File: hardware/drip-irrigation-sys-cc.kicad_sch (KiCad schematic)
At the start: 4 parts

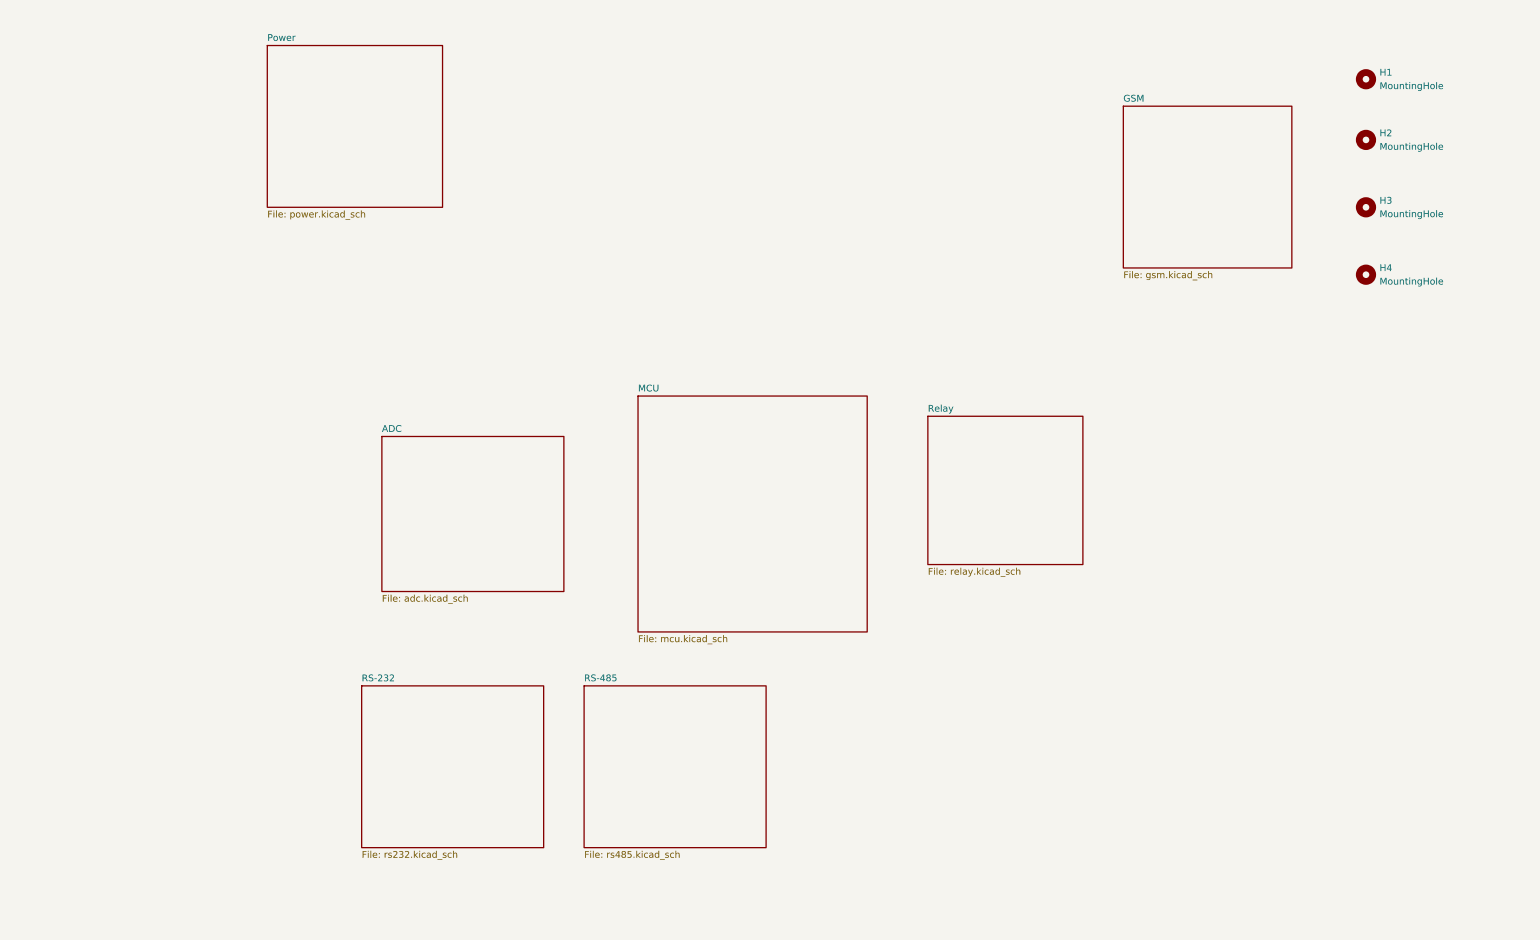
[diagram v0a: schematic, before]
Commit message: power.kicad_sch düzenlemesi yapıldı.
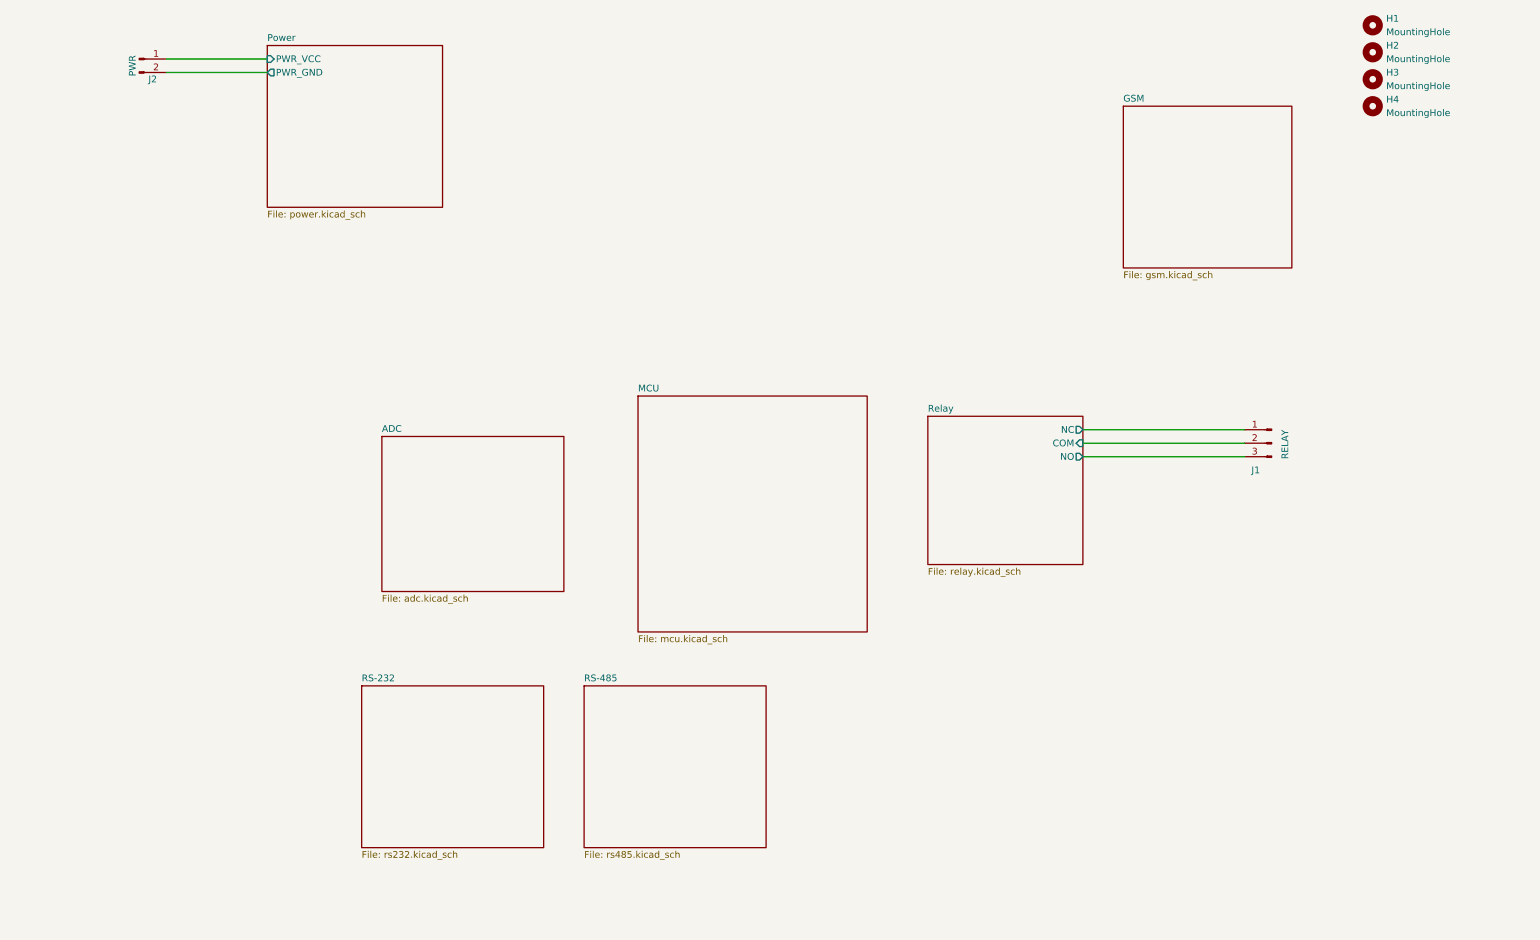
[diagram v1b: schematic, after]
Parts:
- added J1: RELAY, Connector_Phoenix_MSTB:PhoenixContact_MSTBA_2,5_3-G_1x03_P5.00mm_Horizontal, symbol Connector:Conn_01x03_Pin
- added J2: PWR, Connector_Phoenix_MSTB:PhoenixContact_MSTBA_2,5_2-G-5,08_1x02_P5.08mm_Horizontal, symbol Connector:Conn_01x02_Pin
- H1, H2, H3, H4: footprint (none) -> MountingHole:MountingHole_2.5mm
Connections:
- new net Power/PWR_GND: J2.2 (Pin_2)
- new net Power/PWR_VCC: J2.1 (Pin_1)
- new net Relay/COM: J1.2 (Pin_2)
- new net Relay/NC: J1.1 (Pin_1)
- new net Relay/NO: J1.3 (Pin_3)
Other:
- sheet Power ports: added PWR_GND, PWR_VCC; removed none
- sheet Relay ports: added COM, NC, NO; removed none
- moved on the sheet: H1, H2, H3, H4
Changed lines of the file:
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@@
 (kicad_sch (version 20230121) (generator eeschema)
   (paper "A4")
-  (symbol (lib_id "Mechanical:MountingHole") (at 265.43 50.8 0) (unit 1)
-    (in_bom yes) (on_board yes) (dnp no) (fields_autoplaced)
-    (property "Reference" "H3" (at 267.97 49.53 0)
-      (effects (font (size 1.27 1.27)) (justify left))
-    )
-    (property "Value" "MountingHole" (at 267.97 52.07 0)
-      (effects (font (size 1.27 1.27)) (justify left))
-    )
-    (property "Footprint" "" (at 265.43 50.8 0)
-      (effects (font (size 1.27 1.27)) hide)
-    )
-    (property "Datasheet" "~" (at 265.43 50.8 0)
+  (wire (pts (xy 212.09 92.71) (xy 242.57 92.71))
+    (stroke (width 0) (type default))
+  )
+  (wire (pts (xy 212.09 95.25) (xy 242.57 95.25))
+    (stroke (width 0) (type default))
+  )
+  (wire (pts (xy 212.09 97.79) (xy 242.57 97.79))
+    (stroke (width 0) (type default))
+  )
+  (wire (pts (xy 39.37 22.86) (xy 58.42 22.86))
+    (stroke (width 0) (type default))
+  )
+  (wire (pts (xy 39.37 25.4) (xy 58.42 25.4))
+    (stroke (width 0) (type default))
+  )
+  (symbol (lib_id "Mechanical:MountingHole") (at 266.7 26.67 0) (unit 1)
+    (in_bom yes) (on_board yes) (dnp no) (fields_autoplaced)
+    (property "Reference" "H3" (at 269.24 25.4 0)
+      (effects (font (size 1.27 1.27)) (justify left))
+    )
+    (property "Value" "MountingHole" (at 269.24 27.94 0)
+      (effects (font (size 1.27 1.27)) (justify left))
+    )
+    (property "Footprint" "MountingHole:MountingHole_2.5mm" (at 266.7 26.67 0)
+      (effects (font (size 1.27 1.27)) hide)
+    )
+    (property "Datasheet" "~" (at 266.7 26.67 0)
       (effects (font (size 1.27 1.27)) hide)
     )
@@
     )
   )
-  (symbol (lib_id "Mechanical:MountingHole") (at 265.43 63.5 0) (unit 1)
-    (in_bom yes) (on_board yes) (dnp no) (fields_autoplaced)
-    (property "Reference" "H4" (at 267.97 62.23 0)
-      (effects (font (size 1.27 1.27)) (justify left))
-    )
-    (property "Value" "MountingHole" (at 267.97 64.77 0)
-      (effects (font (size 1.27 1.27)) (justify left))
-    )
-    (property "Footprint" "" (at 265.43 63.5 0)
-      (effects (font (size 1.27 1.27)) hide)
-    )
-    (property "Datasheet" "~" (at 265.43 63.5 0)
+  (symbol (lib_id "Connector:Conn_01x02_Pin") (at 34.29 22.86 0) (unit 1)
+    (in_bom yes) (on_board yes) (dnp no)
+    (property "Reference" "J2" (at 36.83 26.67 0)
+      (effects (font (size 1.27 1.27)))
+    )
+    (property "Value" "PWR" (at 33.02 24.13 90)
+      (effects (font (size 1.27 1.27)))
+    )
+    (property "Footprint" "Connector_Phoenix_MSTB:PhoenixContact_MSTBA_2,5_2-G-5,08_1x02_P5.08mm_Horizontal" (at 34.29 22.86 0)
+      (effects (font (size 1.27 1.27)) hide)
+    )
+    (property "Datasheet" "~" (at 34.29 22.86 0)
+      (effects (font (size 1.27 1.27)) hide)
+    )
+    (pin "1")
+    (pin "2")
+    (instances
+      (project "drip-irrigation-sys-cc"
+        (path "/41708c1e-19b2-4374-83f2-108076d82b45"
+          (reference "J2") (unit 1)
+        )
+      )
+    )
+  )
+  (symbol (lib_id "Connector:Conn_01x03_Pin") (at 247.65 95.25 0) (mirror y) (unit 1)
+    (in_bom yes) (on_board yes) (dnp no)
+    (property "Reference" "J1" (at 243.84 100.33 0)
+      (effects (font (size 1.27 1.27)) (justify right))
+    )
+    (property "Value" "RELAY" (at 250.19 92.71 90)
+      (effects (font (size 1.27 1.27)) (justify right))
+    )
+    (property "Footprint" "Connector_Phoenix_MSTB:PhoenixContact_MSTBA_2,5_3-G_1x03_P5.00mm_Horizontal" (at 247.65 95.25 0)
+      (effects (font (size 1.27 1.27)) hide)
+    )
+    (property "Datasheet" "~" (at 247.65 95.25 0)
+      (effects (font (size 1.27 1.27)) hide)
+    )
+    (pin "1")
+    (pin "2")
+    (pin "3")
+    (instances
+      (project "drip-irrigation-sys-cc"
+        (path "/41708c1e-19b2-4374-83f2-108076d82b45"
+          (reference "J1") (unit 1)
+        )
+      )
+    )
+  )
+  (symbol (lib_id "Mechanical:MountingHole") (at 266.7 31.75 0) (unit 1)
+    (in_bom yes) (on_board yes) (dnp no) (fields_autoplaced)
+    (property "Reference" "H4" (at 269.24 30.48 0)
+      (effects (font (size 1.27 1.27)) (justify left))
+    )
+    (property "Value" "MountingHole" (at 269.24 33.02 0)
+      (effects (font (size 1.27 1.27)) (justify left))
+    )
+    (property "Footprint" "MountingHole:MountingHole_2.5mm" (at 266.7 31.75 0)
+      (effects (font (size 1.27 1.27)) hide)
+    )
+    (property "Datasheet" "~" (at 266.7 31.75 0)
       (effects (font (size 1.27 1.27)) hide)
     )
@@
     )
   )
-  (symbol (lib_id "Mechanical:MountingHole") (at 265.43 26.67 0) (unit 1)
-    (in_bom yes) (on_board yes) (dnp no) (fields_autoplaced)
-    (property "Reference" "H1" (at 267.97 25.4 0)
-      (effects (font (size 1.27 1.27)) (justify left))
-    )
-    (property "Value" "MountingHole" (at 267.97 27.94 0)
-      (effects (font (size 1.27 1.27)) (justify left))
-    )
-    (property "Footprint" "" (at 265.43 26.67 0)
-      (effects (font (size 1.27 1.27)) hide)
-    )
-    (property "Datasheet" "~" (at 265.43 26.67 0)
+  (symbol (lib_id "Mechanical:MountingHole") (at 266.7 16.51 0) (unit 1)
+    (in_bom yes) (on_board yes) (dnp no) (fields_autoplaced)
+    (property "Reference" "H1" (at 269.24 15.24 0)
+      (effects (font (size 1.27 1.27)) (justify left))
+    )
+    (property "Value" "MountingHole" (at 269.24 17.78 0)
+      (effects (font (size 1.27 1.27)) (justify left))
+    )
+    (property "Footprint" "MountingHole:MountingHole_2.5mm" (at 266.7 16.51 0)
+      (effects (font (size 1.27 1.27)) hide)
+    )
+    (property "Datasheet" "~" (at 266.7 16.51 0)
       (effects (font (size 1.27 1.27)) hide)
     )
@@
     )
   )
-  (symbol (lib_id "Mechanical:MountingHole") (at 265.43 38.1 0) (unit 1)
-    (in_bom yes) (on_board yes) (dnp no) (fields_autoplaced)
-    (property "Reference" "H2" (at 267.97 36.83 0)
-      (effects (font (size 1.27 1.27)) (justify left))
-    )
-    (property "Value" "MountingHole" (at 267.97 39.37 0)
-      (effects (font (size 1.27 1.27)) (justify left))
-    )
-    (property "Footprint" "" (at 265.43 38.1 0)
-      (effects (font (size 1.27 1.27)) hide)
-    )
-    (property "Datasheet" "~" (at 265.43 38.1 0)
+  (symbol (lib_id "Mechanical:MountingHole") (at 266.7 21.59 0) (unit 1)
+    (in_bom yes) (on_board yes) (dnp no) (fields_autoplaced)
+    (property "Reference" "H2" (at 269.24 20.32 0)
+      (effects (font (size 1.27 1.27)) (justify left))
+    )
+    (property "Value" "MountingHole" (at 269.24 22.86 0)
+      (effects (font (size 1.27 1.27)) (justify left))
+    )
+    (property "Footprint" "MountingHole:MountingHole_2.5mm" (at 266.7 21.59 0)
+      (effects (font (size 1.27 1.27)) hide)
+    )
+    (property "Datasheet" "~" (at 266.7 21.59 0)
       (effects (font (size 1.27 1.27)) hide)
     )
@@
       (effects (font (size 1.27 1.27)) (justify left top))
     )
+    (pin "COM" input (at 212.09 95.25 0)
+      (effects (font (size 1.27 1.27)) (justify right))
+    )
+    (pin "NC" output (at 212.09 92.71 0)
+      (effects (font (size 1.27 1.27)) (justify right))
+    )
+    (pin "NO" output (at 212.09 97.79 0)
+      (effects (font (size 1.27 1.27)) (justify right))
+    )
     (instances
       (project "drip-irrigation-sys-cc"
@@
       (effects (font (size 1.27 1.27)) (justify left top))
     )
-    (instances
+    (pin "PWR_VCC" input (at 58.42 22.86 180)
+      (effects (font (size 1.27 1.27)) (justify left))
+    )
+    (pin "PWR_GND" output (at 58.42 25.4 180)
+      (effects (font (size 1.27 1.27)) (justify left))
+    )
+    (instances

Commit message: Kicad şema düzenlemesi yapıldı.
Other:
- sheet ADC ports: added MCU_ADC, PRESSURE_SENSOR_ANALOG_SIGNAL; removed none
- sheet Relay ports: added 5V_GND, 5V_VCC, MCU_RELAY_PIN; removed none
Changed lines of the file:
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@@
       (effects (font (size 1.27 1.27)) (justify right))
+    )
+    (pin "MCU_RELAY_PIN" output (at 182.88 97.79 180)
+      (effects (font (size 1.27 1.27)) (justify left))
+    )
+    (pin "5V_VCC" output (at 182.88 92.71 180)
+      (effects (font (size 1.27 1.27)) (justify left))
+    )
+    (pin "5V_GND" output (at 182.88 95.25 180)
+      (effects (font (size 1.27 1.27)) (justify left))
     )
     (instances
@@
       (effects (font (size 1.27 1.27)) (justify left top))
     )
+    (pin "PRESSURE_SENSOR_ANALOG_SIGNAL" input (at 80.01 96.52 180)
+      (effects (font (size 1.27 1.27)) (justify left))
+    )
+    (pin "MCU_ADC" output (at 114.3 104.14 0)
+      (effects (font (size 1.27 1.27)) (justify right))
+    )
     (instances

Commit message: Kicad şema düzenlemesi yapıldı.
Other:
- sheet Relay ports: added none; removed 5V_GND, 5V_VCC
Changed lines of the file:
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@@
-      (effects (font (size 1.27 1.27)) (justify left))
-    )
-    (pin "5V_VCC" output (at 182.88 92.71 180)
-      (effects (font (size 1.27 1.27)) (justify left))
-    )
-    (pin "5V_GND" output (at 182.88 95.25 180)
       (effects (font (size 1.27 1.27)) (justify left))
     )

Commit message: Kicad şema düzenlemesi yapıldı.
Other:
- removed sheet GSM
- added sheet mg2608 (mg_2608.kicad_sch)
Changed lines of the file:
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@@
-    )
-  )
-  (sheet (at 219.71 31.75) (size 31.75 30.48) (fields_autoplaced)
-    (stroke (width 0.1524) (type solid))
-    (fill (color 0 0 0 0.0000))
-    (property "Sheetname" "GSM" (at 219.71 31.0384 0)
-      (effects (font (size 1.27 1.27)) (justify left bottom))
-    )
-    (property "Sheetfile" "gsm.kicad_sch" (at 219.71 62.8146 0)
-      (effects (font (size 1.27 1.27)) (justify left top))
-    )
-    (instances
-      (project "drip-irrigation-sys-cc"
-        (path "/41708c1e-19b2-4374-83f2-108076d82b45" (page "7"))
-      )
     )
   )
@@
       )
     )
+  )
+  (sheet (at 205.1812 16.5608) (size 48.9204 34.0868) (fields_autoplaced)
+    (stroke (width 0.1524) (type solid))
+    (fill (color 0 0 0 0.0000))
+    (property "Sheetname" "mg2608" (at 205.1812 15.8492 0)
+      (effects (font (size 1.27 1.27)) (justify left bottom))
+    )
+    (property "Sheetfile" "mg_2608.kicad_sch" (at 205.1812 51.2322 0)
+      (effects (font (size 1.27 1.27)) (justify left top))
+    )
+    (pin "4V" input (at 205.1812 23.8252 180)
+      (effects (font (size 1.27 1.27)) (justify left))
+    )
+    (pin "uart1_rx" input (at 205.1812 32.258 180)
+      (effects (font (size 1.27 1.27)) (justify left))
+    )
+    (pin "uart1_tx" input (at 205.1812 39.1668 180)
+      (effects (font (size 1.27 1.27)) (justify left))
+    )
+    (instances
+      (project "mg2608"
+        (path "/63a0379d-fc16-4019-b887-c3021204e6ee" (page "2"))
+      )
+    )

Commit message: Kicad düzenleme.
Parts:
- added C19: 10nf, symbol Device:C
- added D7: ERROR_LED, symbol Device:LED
- added D8: STATUS_LED, symbol Device:LED
- added D9: POWER_LED, symbol Device:LED
- added J3: PRESSURE_SENSOR, Connector_Phoenix_MSTB:PhoenixContact_MSTBA_2,5_3-G_1x03_P5.00mm_Horizontal, symbol Connector:Conn_01x03_Pin
- added J4: USB_A, symbol Connector:USB_A
- added K2, K3: Relay_SPST-NO, symbol Relay:Relay_SPST-NO
- added R14, R15, R16: 100ohm, symbol Device:R
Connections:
- net ADC/PRESSURE_SENSOR_ANALOG_SIGNAL: now also J3.1 (Pin_1)
- new net: D9.2 (A), R14.2
- new net: K2.13, R15.1
- new net: D8.2 (A), R15.2
- new net: D7.2 (A), R16.1
- new net: K3.13, R16.2
- new net: C19.1, J4.5 (Shield)
- new net +5V: J3.2 (Pin_2), J4.1 (VBUS), K2.14, K3.14, R14.1
- new net GND: C19.2, D7.1 (K), D8.1 (K), D9.1 (K), J3.3 (Pin_3), J4.4 (GND), K2.A2, K3.A2
- new net MCU/MCU_ERROR_LED: K3.A1
- new net MCU/MCU_STATUS_LED: K2.A1
- new net MCU/USB_DM: J4.2 (D-)
- new net MCU/USB_DP: J4.3 (D+)
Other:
- sheet MCU ports: added BTN_ACTIVATE, BTN_DEACTIVATE, BTN_IO, I2C_SCL, I2C_SDA, MCU_ADC_IN, MCU_ERROR_LED, MCU_RELAY, MCU_STATUS_LED, SPI1_MISO, SPI1_MOSI, SPI1_SCK, SYS_JTCK_SWCLK, SYS_JTMS_SWDIO, UART_RX, UART_TX, USAR1_RX, USART1_TX, USART2_RX, USART2_TX, USART3_RX, USART3_TX, USB_DM, USB_DP; removed none
- sheet Power ports: added 5V; removed none
- sheet mg2608 ports: added 5V_INPUT; removed 4V

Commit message: Kicad şema düzenlemesi yapıldı.
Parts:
- removed K2, K3: Relay_SPST-NO, symbol Relay:Relay_SPST-NO
- C19: footprint (none) -> Capacitor_SMD:C_1206_3216Metric; Digikey (none) -> 5440-FN31X103K500PXGTR-ND
- D7: footprint (none) -> LED_SMD:LED_1206_3216Metric; Digikey (none) -> 754-AP3216IDTR-ND
- D8, D9: footprint (none) -> LED_SMD:LED_0603_1608Metric; Digikey (none) -> 67-SML-LXFT0603GC-TR-ND
- R14, R15, R16: value 100ohm -> 330ohm
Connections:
- net MCU/MCU_ERROR_LED: now also R16.1
- net MCU/MCU_STATUS_LED: now also R15.2
- net at R15.1: now also D8.2 (A)
- net at D7.2 (A): now also R16.2; no longer R16.1
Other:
- removed sheet mg2608
- added sheet GSM_Module (gsm_module.kicad_sch)
- sheet RS-232 ports: added RS232_RX, RS232_TX; removed none
- sheet RS-485: file rs485.kicad_sch -> rs232-rs485.kicad_sch
- sheet RS-485 ports: added RS485_A, RS485_B; removed none
- moved on the sheet: R15, R16

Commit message: Kicad şema düzenlemesi yapıldı.
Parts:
- added C7, C8, C9: 100nf, Capacitor_SMD:C_0201_0603Metric, symbol Device:C_Small
- added J8: UJ2-AV-4-SMT-TR, CONN4X1_UJ2-AV-4-SMT-TR_CUD, symbol drip-irrigation-sys-cc:UJ2-AV-4-SMT-TR
- added J9: Conn_02x01, Connector_PinHeader_1.00mm:PinHeader_1x02_P1.00mm_Vertical, symbol Connector_Generic:Conn_02x01
- added R1, R3, R5: 10K, Resistor_SMD:R_0402_1005Metric, symbol Device:R
- added R2, R4, R6: 1K, Resistor_SMD:R_0603_1608Metric, symbol Device:R
- added SW1: BTN_DEACTIVE, SW_PTS636_CNK, symbol drip-irrigation-sys-cc:PTS636_SM50J_SMTR_LFS
- added SW2: BTN_IO, SW_PTS636_CNK, symbol drip-irrigation-sys-cc:PTS636_SM50J_SMTR_LFS
- added SW3: BTN_ACTIVE, SW_PTS636_CNK, symbol drip-irrigation-sys-cc:PTS636_SM50J_SMTR_LFS
- J4: footprint (none) -> drip-irrigation-sys-cc:CONN4X1_UJ2-AV-4-SMT-TR_CUD
- R14, R15, R16: footprint (none) -> Resistor_SMD:R_0402_1005Metric; Digikey (none) -> 2577-AS02FTE3300TR-ND
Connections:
- net +5V: now also R1.2, R3.2, R5.2
- net GND: now also C7.1, C8.1, C9.1, SW1.2, SW2.2, SW3.2
- net MCU/BTN_ACTIVATE: now also C8.2, R3.1, R4.1
- net MCU/BTN_DEACTIVATE: now also C7.2, R1.1, R2.1
- net MCU/BTN_IO: now also C9.2, R5.1, R6.1
- new net: R2.2, SW1.1
- new net: R4.2, SW2.1
- new net: R6.2, SW3.1
- new net RS-232/RS232_RX: J9.1 (Pin_1)
- new net RS-232/RS232_TX: J9.2 (Pin_2)
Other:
- added sheet EXP (exp.kicad_sch)
- sheet MCU ports: added none; removed SYS_JTCK_SWCLK, SYS_JTMS_SWDIO
- sheet RS-232 ports: added USART1_RX, USART1_TX; removed none
